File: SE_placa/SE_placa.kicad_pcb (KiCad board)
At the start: 2 copper layers, 66 parts, among them IC1 TP4056, J1 5V, J2 Micro_SD_Card_Det_Hirose_DM3AT, J3 Conn_02x07_ESP32_IO, J4 I2C-0, J5 I2C-1, J6 Conn_02x03_LORA_IO, J7 U.FL-R-SMT(01), J8 UART, J9 Connector Bateria, Q1 BSS138, Q2 BSS138, SW1 SW_Push_Download, SW2 SW_Push_ESP_RST, U1 ESP32-WROVER, U2 RFM95W-915S2, U3 LTC3441EDEPBF

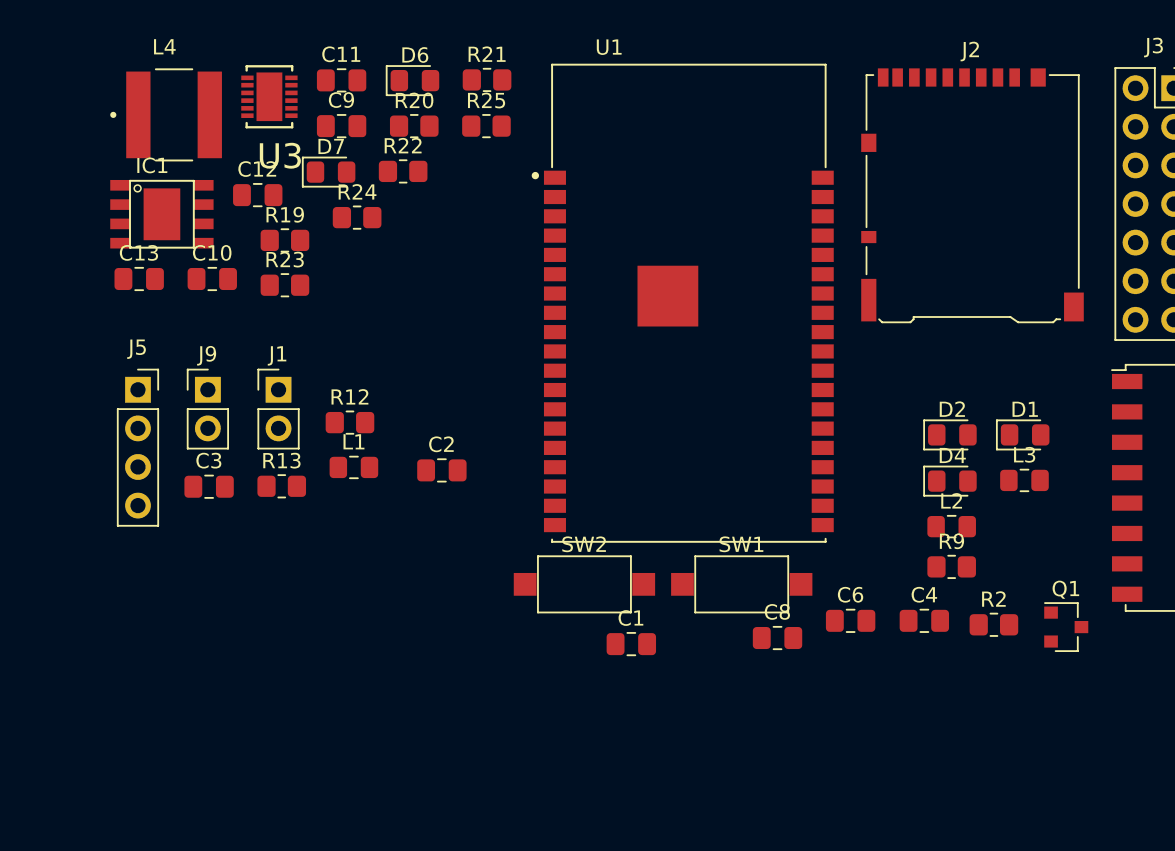
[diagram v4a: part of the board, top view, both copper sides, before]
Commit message: Inclusion informacion ref SINK SOURCE
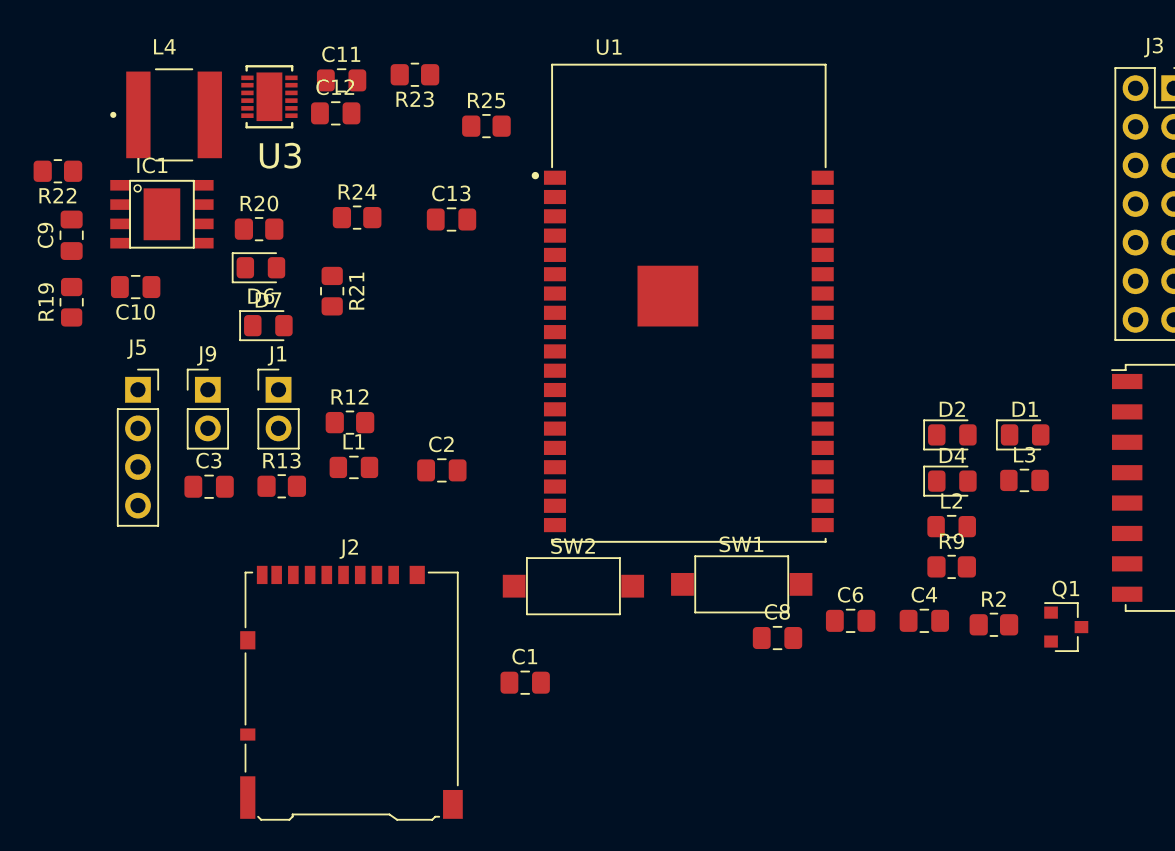
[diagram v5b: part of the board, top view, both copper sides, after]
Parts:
- moved J2 52.4 mm to (127.6, 69.2)
- moved R22 22.7 mm to (108.3, 34.9), turned to 180 degrees
- moved C13 20.9 mm to (134.2, 38.1)
- moved C9 19.2 mm to (109.2, 39.1), turned to 90 degrees
- moved R21 17.2 mm to (126.4, 42.8), turned to 270 degrees
- moved R23 16.3 mm to (131.8, 28.6), turned to 180 degrees
- moved D6 15.9 mm to (121.7, 41.3)
- moved R19 14.6 mm to (109.2, 43.5), turned to 90 degrees
- moved R20 12.3 mm to (121.6, 38.7)
- moved D7 10.9 mm to (122.2, 45.1)
- moved C12 7.44 mm to (126.6, 31.1)
- moved C1 7.43 mm to (139.1, 68.6)
- moved C10 5.07 mm to (113.4, 42.5), turned to 180 degrees
- moved SW2 0.73 mm to (142.2, 62.2)

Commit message: Organizar integrado rev A
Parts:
- moved J5 97.0 mm to (209.6, 63.5)
- moved R13 79.1 mm to (200.4, 72.4)
- moved R12 75.1 mm to (200.7, 68.6)
- moved J8 59.4 mm to (149.9, 72.4), turned to 90 degrees
- moved J3 58.4 mm to (142.2, 72.4), turned to 270 degrees
- moved R8 56.9 mm to (142.2, 47.0), turned to 180 degrees
- moved R18 52.9 mm to (244.6, 79.8)
- moved R7 52.9 mm to (249.3, 67.9)
- moved C5 52.9 mm to (248.5, 60.4)
- moved C7 52.9 mm to (241.4, 65.0)
- moved D3 52.9 mm to (232.2, 70.6)
- moved D5 52.9 mm to (232.2, 67.6)
- moved J6 52.9 mm to (243.8, 56.1)
- moved J7 52.9 mm to (248.9, 55.9)
- moved R1 52.9 mm to (236.9, 68.0)
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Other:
- board outline added: 114.3 x 50.8 mm

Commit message: Update SE_placa.kicad_pcb
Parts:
- moved R11 106.0 mm to (146.1, 36.8), turned to 90 degrees
- moved R17 73.8 mm to (178.5, 43.8)
- moved R18 73.8 mm to (178.5, 46.8)
- moved R16 66.0 mm to (185.4, 57.4), turned to 270 degrees
- moved D3 61.4 mm to (178.9, 40.1)
- moved D5 61.4 mm to (178.9, 37.1)
- moved R1 61.4 mm to (183.6, 37.5)
- moved R4 61.4 mm to (183.6, 40.5)
- moved R15 57.4 mm to (192.5, 49.8)
- moved R14 52.2 mm to (201.7, 54.4)
- moved R7 52.2 mm to (199.8, 51.4)
- moved R3 50.1 mm to (197.1, 54.8), turned to 90 degrees
- moved C7 44.6 mm to (197.1, 59.6), turned to 90 degrees
- moved J7 39.0 mm to (212.1, 43.2)
- moved C5 38.2 mm to (212.3, 48.3)
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
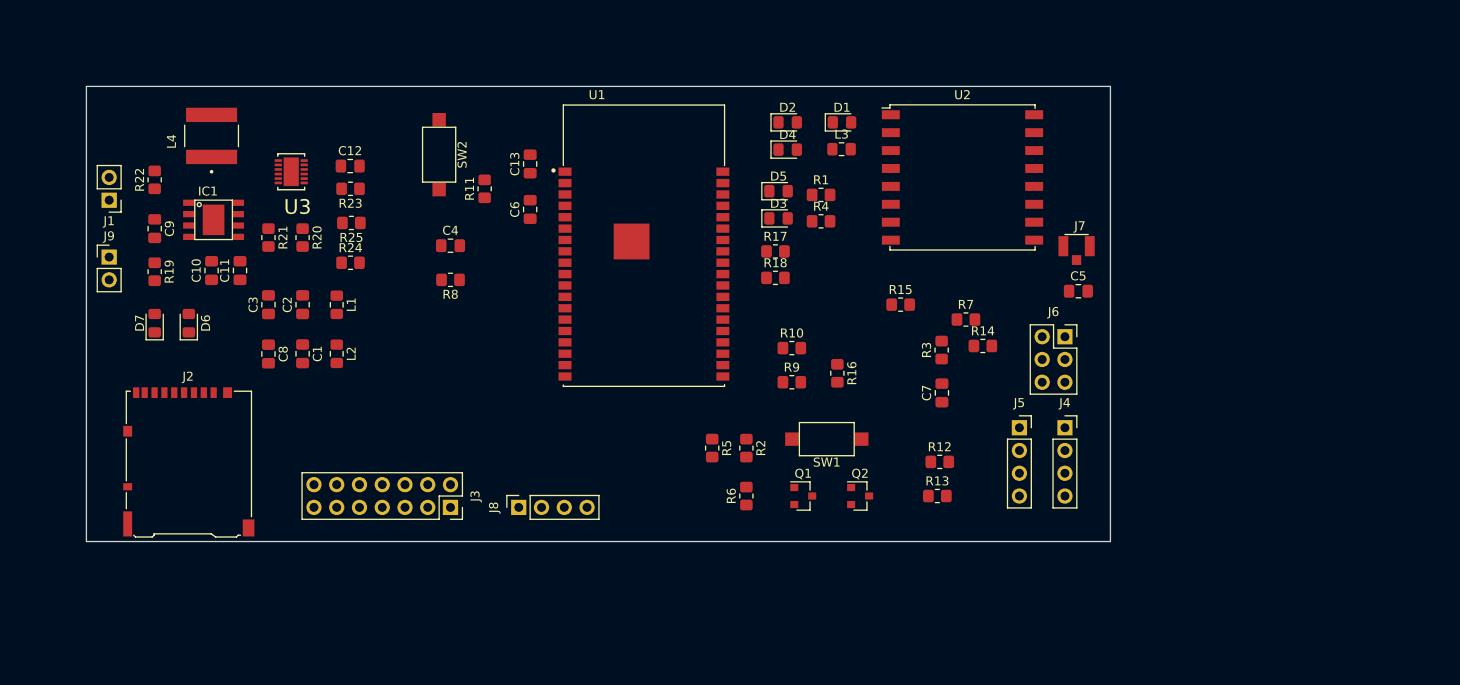
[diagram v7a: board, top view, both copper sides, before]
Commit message: ruteo 1
1. Agregados mounting holes 2.5 mm
2. Reordeno elementos para hacer mas facil el ruteo.
3. Ordeno los leds para indicar mejor el estado de lora y alimentacion general
4. Ordeno lesd y conectores de bateria y alimentacion por panel
giro conectores de I/o de lora
en general se dejaron por grupos los elementos de acuerdo al tipo de funcion dentro de la placa
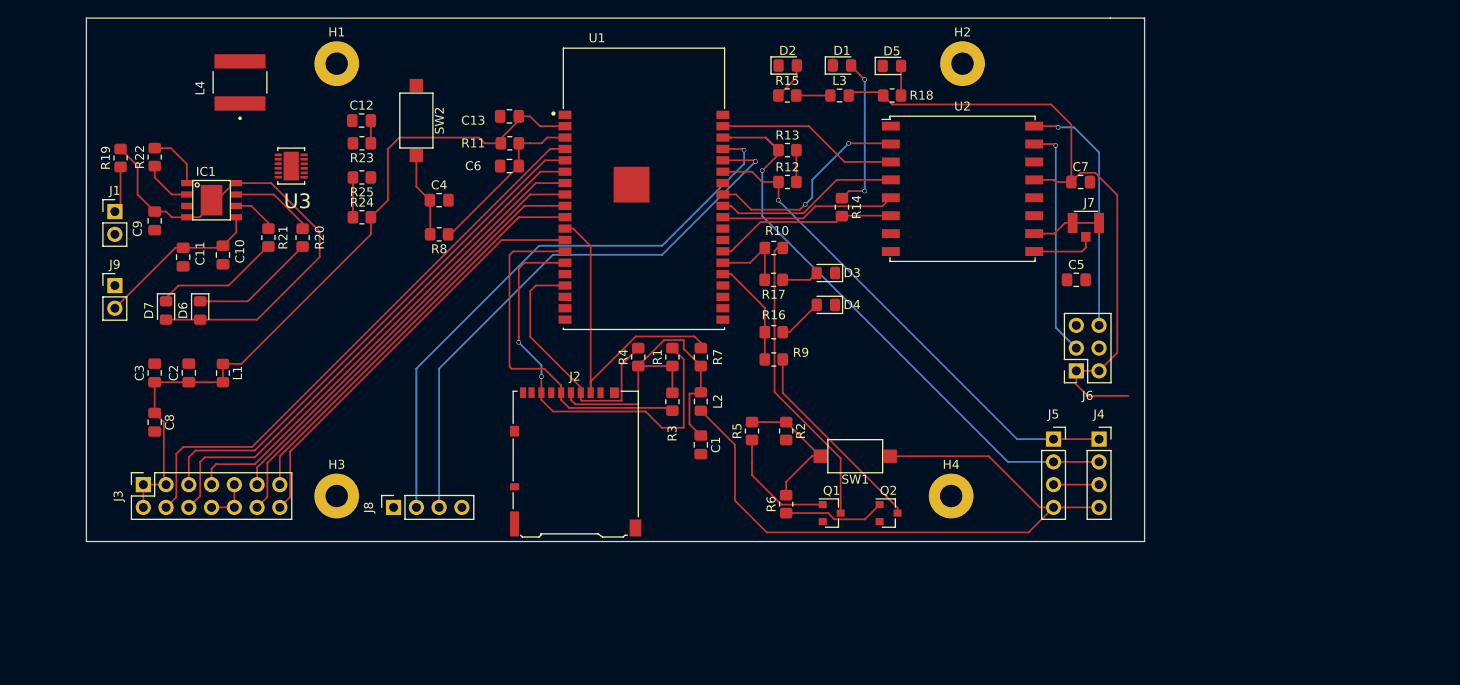
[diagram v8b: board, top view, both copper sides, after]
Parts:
- added H1: MountingHole, MountingHole:MountingHole_2.5mm_Pad, F.Cu at (129.5, 22.9)
- added H2: MountingHole, MountingHole:MountingHole_2.5mm_Pad, F.Cu at (199.4, 22.9)
- added H3: MountingHole, MountingHole:MountingHole_2.5mm_Pad, F.Cu at (129.5, 71.1)
- added H4: MountingHole, MountingHole:MountingHole_2.5mm_Pad, F.Cu at (198.1, 71.1)
- moved C1 45.6 mm to (170.2, 65.4)
- moved J2 43.2 mm to (156.2, 67.3)
- moved R13 42.1 mm to (179.8, 32.5)
- moved L2 41.0 mm to (170.2, 60.6)
- moved R12 35.6 mm to (179.8, 36.1)
- moved J3 34.4 mm to (108.0, 69.8), turned to 90 degrees
- moved R3 30.6 mm to (167.0, 60.6), turned to 270 degrees
- moved R7 29.9 mm to (170.2, 55.6), turned to 90 degrees
- moved C7 28.2 mm to (212.6, 36.1), turned to 0 degrees
- moved R15 26.6 mm to (179.8, 26.4)
- moved R4 25.4 mm to (163.2, 55.6), turned to 90 degrees
- moved R1 24.6 mm to (167.0, 55.6), turned to 90 degrees
- moved R18 24.2 mm to (191.5, 26.4), turned to 180 degrees
- moved R14 22.1 mm to (185.9, 38.9), turned to 270 degrees
- moved D5 18.9 mm to (191.5, 23.1)
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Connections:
- J3 pad 10: Net-(J3-Pad10) -> GND
- J3 pad 8: Net-(J3-Pad10) -> GND
- J3 pad 9: Net-(J3-Pad10) -> GND
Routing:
- net +3V3: track 0.00 -> 165.7 mm
- net +3.3VP: track 0.00 -> 74.5 mm
- net /I2C-SCL: track 0.00 -> 66.6 mm, vias 0 -> 1
- net /TXD0: track 0.00 -> 65.5 mm, vias 0 -> 1
- net /RXD0: track 0.00 -> 64.1 mm, vias 0 -> 1
- net /I36: track 0.00 -> 63.9 mm
- net /I34: track 0.00 -> 59.7 mm
- net /I39: track 0.00 -> 58.8 mm
- net /I2C-SDA: track 0.00 -> 55.6 mm, vias 0 -> 1
- net /I35: track 0.00 -> 54.4 mm
- net Net-(C9-Pad1): track 0.00 -> 54.3 mm
- net /IO33: track 0.00 -> 50.5 mm
- net /IO32: track 0.00 -> 48.9 mm
- net /SPI2-MISO: track 0.00 -> 47.7 mm, vias 0 -> 2
- net /IO12: track 0.00 -> 47.2 mm
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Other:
- board size 114.3 x 50.8 mm -> 118.1 x 58.4 mm
- net class Default: clearance 0.3 -> 0.2; trace_width 0.25 -> 0.2; via_dia 0.8 -> 0.5
- net class PWR: clearance 0.3 -> 0.2; trace_width 0.5 -> 0.2; via_dia 0.8 -> 0.5
- rule trace_clearance: 0.3 -> 0.2
